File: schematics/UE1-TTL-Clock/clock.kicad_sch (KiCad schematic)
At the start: 11 parts, among them U1 74LS74, U2 74LS08, U3 NE555

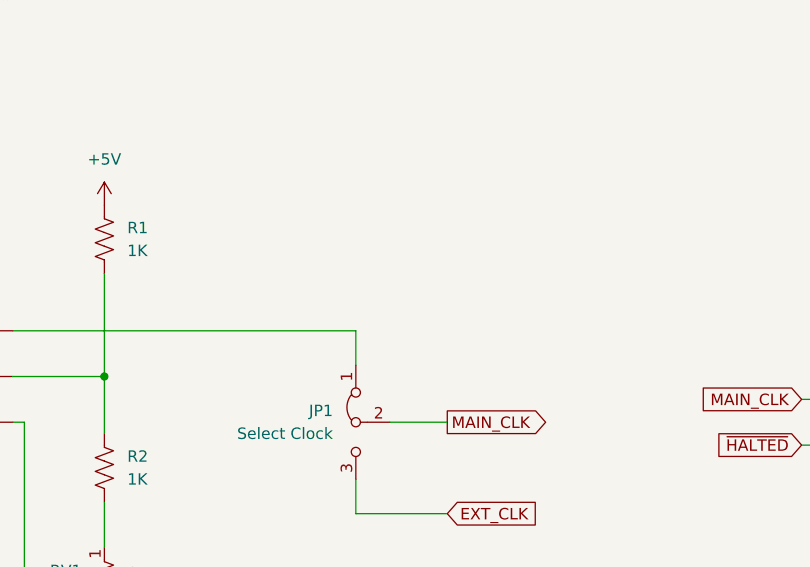
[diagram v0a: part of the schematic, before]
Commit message: Lay out clock board
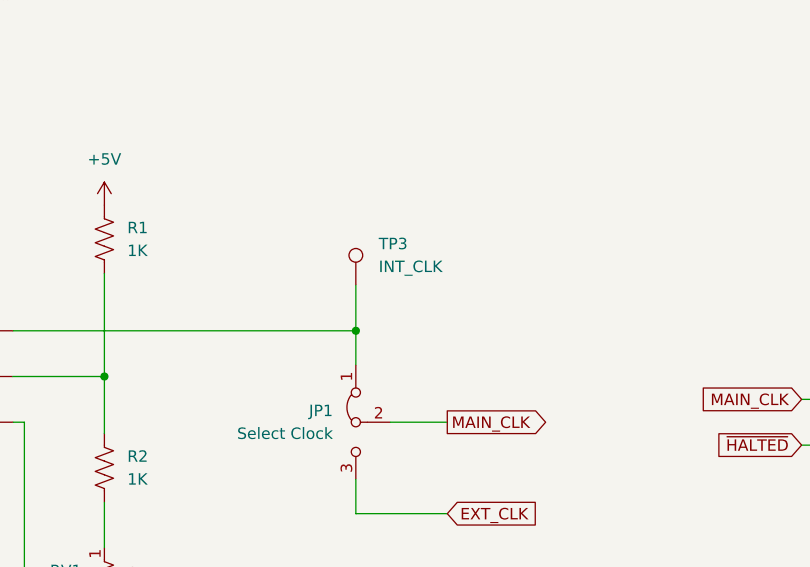
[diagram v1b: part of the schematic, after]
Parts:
- added TP3: INT_CLK, TestPoint:TestPoint_Pad_D1.5mm, symbol Connector:TestPoint
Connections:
- net at JP1.1 (A), U3.3 (Q): now also TP3.1
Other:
- title: UE1- TTL Clock and Diagnostics -> UE1-TTL Clock and Front Panel
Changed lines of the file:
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@@
 	(paper "A4")
 	(title_block
-		(title "UE1- TTL Clock and Diagnostics")
+		(title "UE1-TTL Clock and Front Panel")
 		(date "2025")
 		(rev "1")
@@
 	)
 	(junction
+		(at 123.19 73.66)
+		(diameter 0)
+		(color 0 0 0 0)
+	)
+	(junction
 		(at 86.36 111.76)
 		(diameter 0)
@@
 	(no_connect
 		(at 118.11 173.99)
+	)
+	(wire
+		(pts
+			(xy 123.19 68.58) (xy 123.19 73.66)
+		)
+		(stroke
+			(width 0)
+			(type default)
+		)
 	)
 	(polyline
@@
 				)
 			)
+		)
+	)
+	(symbol
+		(lib_id "Connector:TestPoint")
+		(at 123.19 68.58 0)
+		(unit 1)
+		(exclude_from_sim no)
+		(in_bom yes)
+		(on_board yes)
+		(dnp no)
+		(fields_autoplaced yes)
+		(property "Reference" "TP3"
+			(at 125.73 64.0079 0)
+			(effects
+				(font
+					(size 1.27 1.27)
+				)
+				(justify left)
+			)
+		)
+		(property "Value" "INT_CLK"
+			(at 125.73 66.5479 0)
+			(effects
+				(font
+					(size 1.27 1.27)
+				)
+				(justify left)
+			)
+		)
+		(property "Footprint" "TestPoint:TestPoint_Pad_D1.5mm"
+			(at 128.27 68.58 0)
+			(effects
+				(font
+					(size 1.27 1.27)
+				)
+				(hide yes)
+			)
+		)
+		(property "Datasheet" "~"
+			(at 128.27 68.58 0)
+			(effects
+				(font
+					(size 1.27 1.27)
+				)
+				(hide yes)
+			)
+		)
+		(property "Description" "test point"
+			(at 123.19 68.58 0)
+			(effects
+				(font
+					(size 1.27 1.27)
+				)
+				(hide yes)
+			)
+		)
+		(pin "1"
+		)
+		(instances
+			(project "UE1-TTL-Clock"
+				(path "/3387ba40-0694-43b2-a156-d12ce9552f1f/a8e742c2-4ecc-4032-b987-2be252c4302f"
+					(reference "TP3")
+					(unit 1)
+				)
+			)
